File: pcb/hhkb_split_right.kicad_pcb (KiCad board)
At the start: 2 copper layers, 173.7 x 97.4 mm, 92 parts, among them SW1 6, SW10 Y, SW11 U, SW12 I, SW13 O, SW14 P, SW15 [, SW16 ], SW17 Del, SW18 H, SW19 J, SW2 7, SW20 K, SW21 L, SW22 ;, SW23 ', SW24 Enter, SW25 N, SW26 M, SW27 ,, SW28 ., SW29 /, SW3 8, SW30 Shift, SW31 Fn, SW32 R-Space, SW33 Meta, SW34 Alt, SW4 9, SW5 0, SW6 -, SW7 =, SW8 \, SW9 `, U1 74LVC595, U2 74LVC595

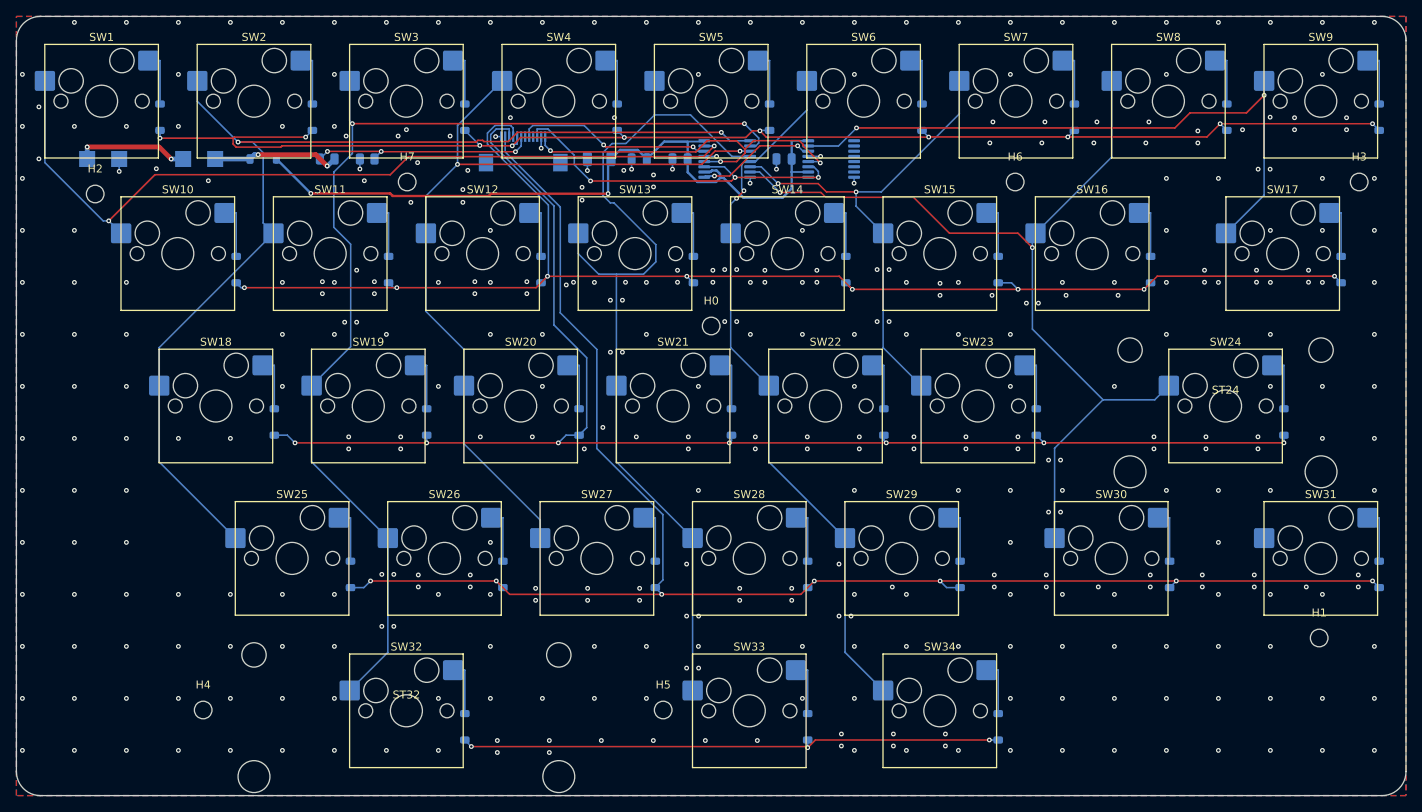
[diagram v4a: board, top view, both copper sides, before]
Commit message: 閾値を設計規則から導き、「厳しすぎ」を検出する検査を足した
利用者の問い「その閾値はヒューリスティックか。妥当か。例外はないか」への対応。

**問題は「緩すぎ」ではなく「厳しすぎ」だった。**
DRC は規則より緩ければ必ず捕まえる（無条件に太らせて 47 件出ることを
故意に壊して確認済み）。だが**規則より厳しく置いても DRC は緑のまま**で、
ビアが減っていても誰も気づけない。実際そうなっていた。

  - クリアランス 0.2 を**数値リテラルで 4 か所**に持っていた。
    設計規則を変えても追随しない
  - ビアの半径を二重に数えていて 0.3mm 過剰に厳しく、
    **10.8mm² の離島でも格子点 48 個が全部「置けない」判定**だった

直した内容:

  - `_clearance_mm(board)` が基板の設計規則から読む。**数値を書かない**
  - `_via_keepout_mm(board)` = ビア半径 + クリアランス + 余裕。
    判断で置いた数字は `SAFETY_MM = 0.05` だけ（丸めと矩形近似の保険）
  - **結果の量を測る検査**を足した。「厳しすぎ」はここでしか見つからない

        test_there_are_enough_ground_vias_to_tie_the_two_planes
        test_few_pieces_of_ground_copper_are_left_floating

効果（判定を直したことによる実測の変化）:

    浮いた GND の区画   左 15 → 4   右 14 → 5
    GND ビアの総数      左 305 → 342   右 396 → 423

**設計規則の数値を tools/pcb_rules.py へ出した。**
gen_pcb は `import pcbnew` するので KiCad の Python でしか読めず、
母艦の venv で動く検査から参照すると ModuleNotFoundError で落ちる。
（`part_kinds.py` を作ったのと同じ理由）

**電源をクラスの幅まで後から引き上げるのはやめた。**
一度やったら DRC 違反が増えた（左 0→1・右 1→2）。分布を測ると:

    VBATT_RAW / VBATT_SW   100% が 0.60mm
    V3V3                   97%（254/261）が 0.30mm、狭い 7 区間だけ 0.225mm

**Freerouting は狭いところで自分から幅を絞っている。**利用者が求めた
「太くできるところは太く、できないところはしない」を自動配線器が
既にやっており、後から一律に太らせるのはその判断を壊す行為だった。

検査側の不具合も 1 つ直した。KiCad 10 はビアのネットを `(net "COL0")` と
**名前**で書く（番号ではない）。番号を期待した正規表現が 1 件も拾えず
「GND のビアが 0 個」という嘘の赤を出していた。S 式を正規表現で読むのを
やめ、pcbnew から取るようにした。

4 層前提の `test_the_ground_stays_one_island_after_routing` は削除。
2 層では信号層とベタが同じ面を兼ねるので**面が割れるのは避けられず、
「島が 1 つ」は達成し得ない条件**になった。割れていてもビアで
繋がっていればよいので、浮いた区画の数で見る検査に置き換えた。

Co-Authored-By: Claude Sonnet 5 <noreply@anthropic.com>
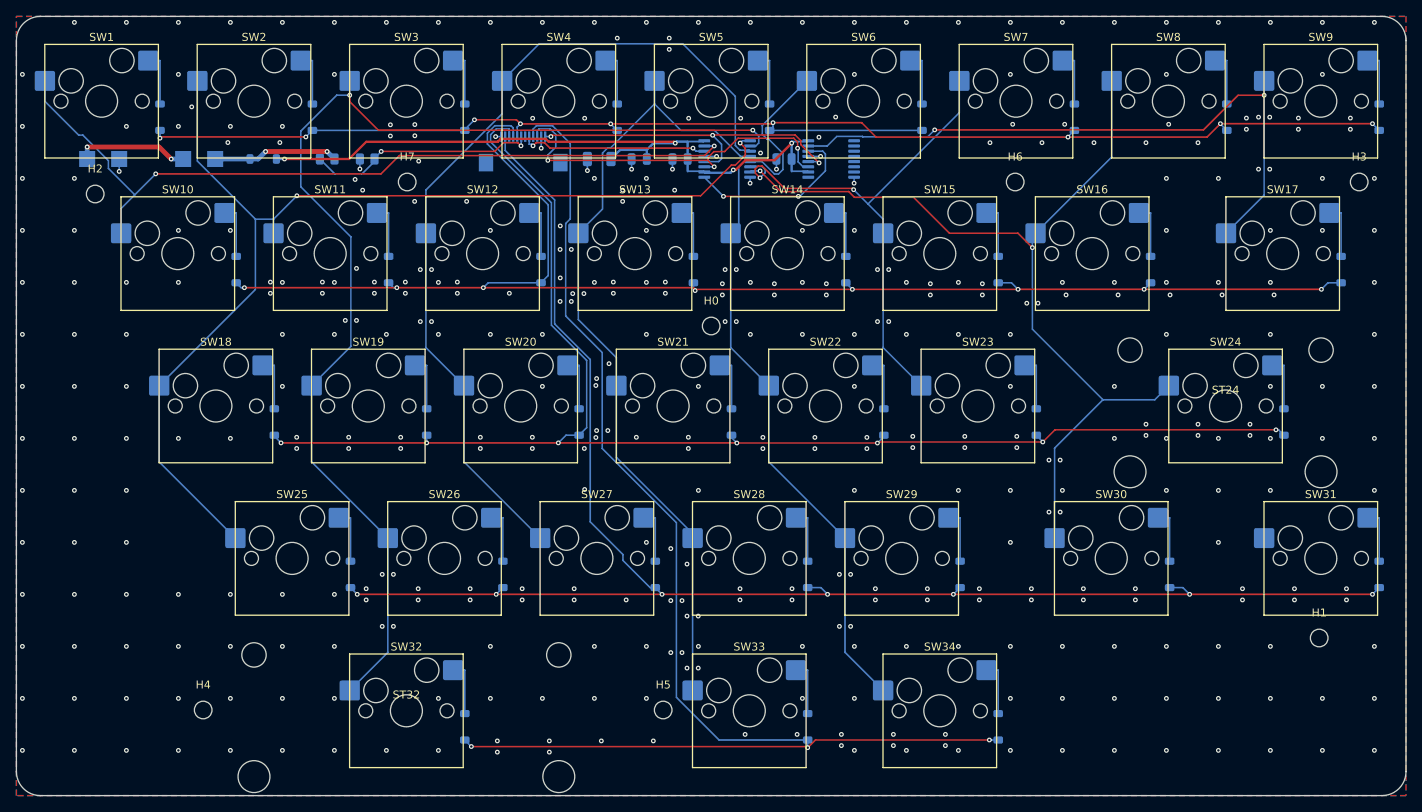
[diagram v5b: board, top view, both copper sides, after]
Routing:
- net ROW4: track 68.4 -> 168.9 mm
- net COL4: track 113.3 -> 100.9 mm
- net U1_U2: track 14.9 -> 21.8 mm
- net COL2: track 139.5 -> 146.0 mm
- net COL5: track 89.1 -> 95.0 mm, vias 2 -> 0
- net ROW1: track 175.3 -> 180.9 mm
- net COL3: track 104.3 -> 109.1 mm, vias 2 -> 0
- net ROW0: track 177.1 -> 181.9 mm, vias 10 -> 9
- net COL6: track 63.2 -> 66.5 mm
- net COL0: track 104.2 -> 100.9 mm
- net CS: track 46.1 -> 43.2 mm
- net V3V3: track 93.4 -> 91.1 mm, vias 2 -> 4
- net COL1: track 137.1 -> 138.5 mm
- net SPI_MOSI: track 24.4 -> 23.5 mm
- net VBATT_SENSE: track 28.3 -> 29.1 mm, vias 3 -> 2
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
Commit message: 浮いた GND を 0 個にした。「消す」前に「繋ぐ」を尽くす（指摘 4/5）
利用者の指摘「0 は理想ではなく必達では。GND のレベルが違う可能性が
あるというのは致命的では」への対応。**指摘が正しく、私が誤っていた。**

私は「現実に 0 にできないので、増加を検出する用途に留める」と書いた。
これは事実に反する。**取り得る手は常に 2 つあり、どちらかは必ず選べる。**

  1. 繋ぐ  ビアが入るなら
  2. 消す  ビアが入らないなら、その銅を残す理由が無い

浮いた銅は電位が定義されておらず GND ではない。遮蔽の役に立たず、
囲んでいる配線どうしを容量結合させ、2.4GHz では再放射する。
**残す利益がゼロ**なので 0 を必達にした（MAX_FLOATING_ISLANDS = 0）。

★ その過程で、繋げるものまで捨てていたバグを 2 つ見つけた。

(1) **島の削除が先に走り、繋ぐ機会が無かった**
    ゾーンを ALWAYS にした結果、**塗った瞬間に浮いた区画が消える**。
    消えたあとに探しても見つからないので、離島に打ったビアは常に 0 だった。
    正しい順序に直した: 削除を止めて塗る → 置けるものにビアを打つ →
    削除を戻して塗る。**23.80mm²（3.76 x 9.75mm）の区画が救われた。**

(2) **探索が 0.5mm 刻みで、置ける場所を見落としていた**
    上記 23.80mm² には 0.1mm 刻みなら 512 点の置ける場所があった。

**刻みという調整値そのものを無くした。**標本化をやめ、幾何で解く。

    区画 − （障害物を「ビア半径＋クリアランス」だけ膨らませたもの）

残りが空でなければ置ける。空ならどうやっても置けない。
「細かく調べれば見つかるかも」が原理的に無くなる。

その実装でも 1 回間違えた。引き算のあとさらに区画の縁から Deflate して
おり、**クリアランスを二重に課していた**（標本化なら 24 点置ける区画を
「置けない」と誤判定）。ビアは区画の内側に丸ごと収まる必要が無い——
区画も GND、ビアも GND なので、守るべきは他ネットとの距離だけ。
直した結果、**45 区画すべてで幾何と標本化が一致（不一致 0）。**

最終状態:

    浮いた区画    左 0 個 / 右 0 個
    消した銅      左 28.4mm2（ベタの 0.13%）/ 右 57.5mm2（0.21%）
    離島に打ったビア 左 2 個 / 右 3 個

消したものは全て、幾何で「ビアが入らない」ことを証明済み。内訳は
スイッチ内部の 0.61x0.65mm の小片（約 30 個）と、幅 0.25〜0.7mm の
細長い帯。**ビアは直径 1.1mm 要るので物理的に入らない。**

Co-Authored-By: Claude Sonnet 5 <noreply@anthropic.com>
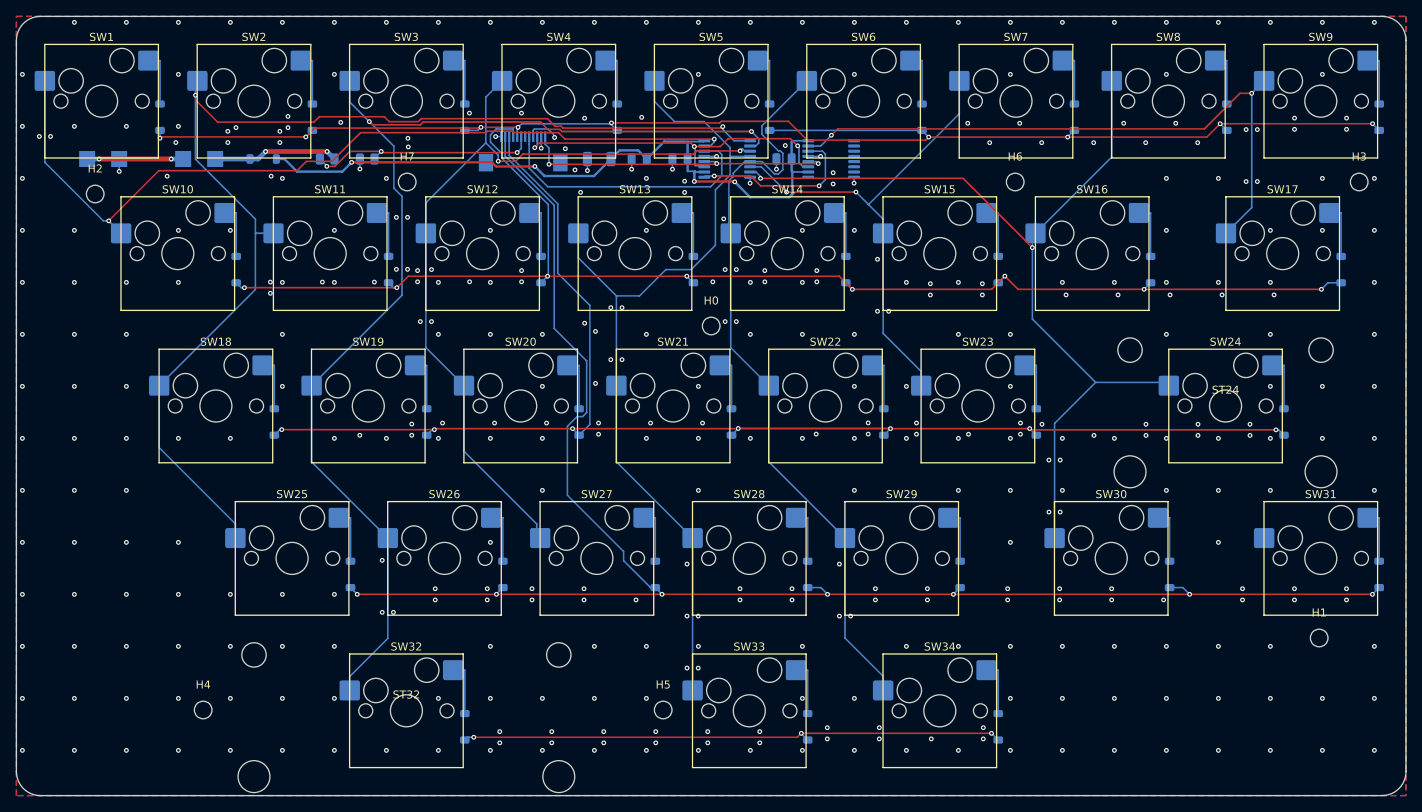
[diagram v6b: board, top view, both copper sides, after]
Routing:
- net ROW4: track 168.9 -> 72.6 mm, vias 3 -> 4
- net SPI_MOSI: track 23.5 -> 34.6 mm, vias 2 -> 0
- net ROW1: track 180.9 -> 173.3 mm
- net COL4: track 100.9 -> 108.0 mm
- net ROW2: track 181.9 -> 174.9 mm
- net COL3: track 109.1 -> 102.2 mm, vias 0 -> 2
- net COL1: track 138.5 -> 144.8 mm
- net COL0: track 100.9 -> 106.0 mm
- net COL2: track 146.0 -> 141.1 mm
- net COL6: track 66.5 -> 62.3 mm
- net SPI_SCK: track 46.3 -> 42.8 mm
- net CS: track 43.2 -> 40.4 mm
- net ROW0: track 181.9 -> 184.7 mm
- net ROW3: track 203.1 -> 205.4 mm
- net VBATT_RAW: track 14.1 -> 12.0 mm
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
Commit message: ★ 斜めのバスにビアが 1 本も立っていなかった（指摘 5 が効いていなかった）
利用者が B.Cu の絵を見て「明らかに斜め線のところにビアがない」と指摘。
調べたら**私の実装に 3 つの欠陥**があった。どれも DRC では出ない。

**(1) 「長い配線」を線分 1 本の長さで判定していた**
列のバスのような斜めの経路は、キーごとの短い線分の連なりでできている。
COL0 は合計 152mm あるのに 10mm 以上の線分は 4 本しかない。
**全 406 本のうち 87%（355 本）が対象外**になっていた。
→ ネットが同じ面に持つ**経路の合計長**で見るようにした。

**(2) 配線を外接矩形で避けていた**
斜めの配線の外接矩形は対角線を含む巨大な長方形になる。つまり
**斜め線の周囲一帯が「置けない」**ことになり、一番ビアが要る場所に
1 本も立たなかった。格子のスティッチングが 8 割方失敗していたのも同じ原因。
→ 線分として点との距離で見るようにした（_near_segment）。

**(3) 順序が逆だった**
埋め草の格子を先に打っていたため、配線の脇という一番効く場所が
先取りされていた。→ 狙って打つフェンスを先に、格子を後に。

利用者の「配線は線分しかないのですか？色々曲がったりするでしょうに」で
**円弧（PCB_ARC）を黙って除外していた**ことも判明。いまの基板に円弧は
0 本（Freerouting は直線しか出さない）が、KiCad で手直しすれば生じる。
_as_segments が円弧を弦に割って扱うようにした。

結果（GND ビアの総数）:

    左  9 → **732 個**（うちフェンス 545）
    右 12 → **913 個**（うちフェンス 662）

DRC は 3 基板とも違反 0（右に 2 件出たのは Freerouting 自身の丸め。
DSN のクリアランスに 10µm 上乗せして解消済み）。

**編集を重ねた結果、gnd_fanout.py に関数が 9 個も二重定義されていた。**
後半が前半を上書きしていて動作はしていたが、重複を削除した。
使わなくなった widen も消した（CLAUDE.md「置き換えたら古い方を消す」）。

Co-Authored-By: Claude Sonnet 5 <noreply@anthropic.com>
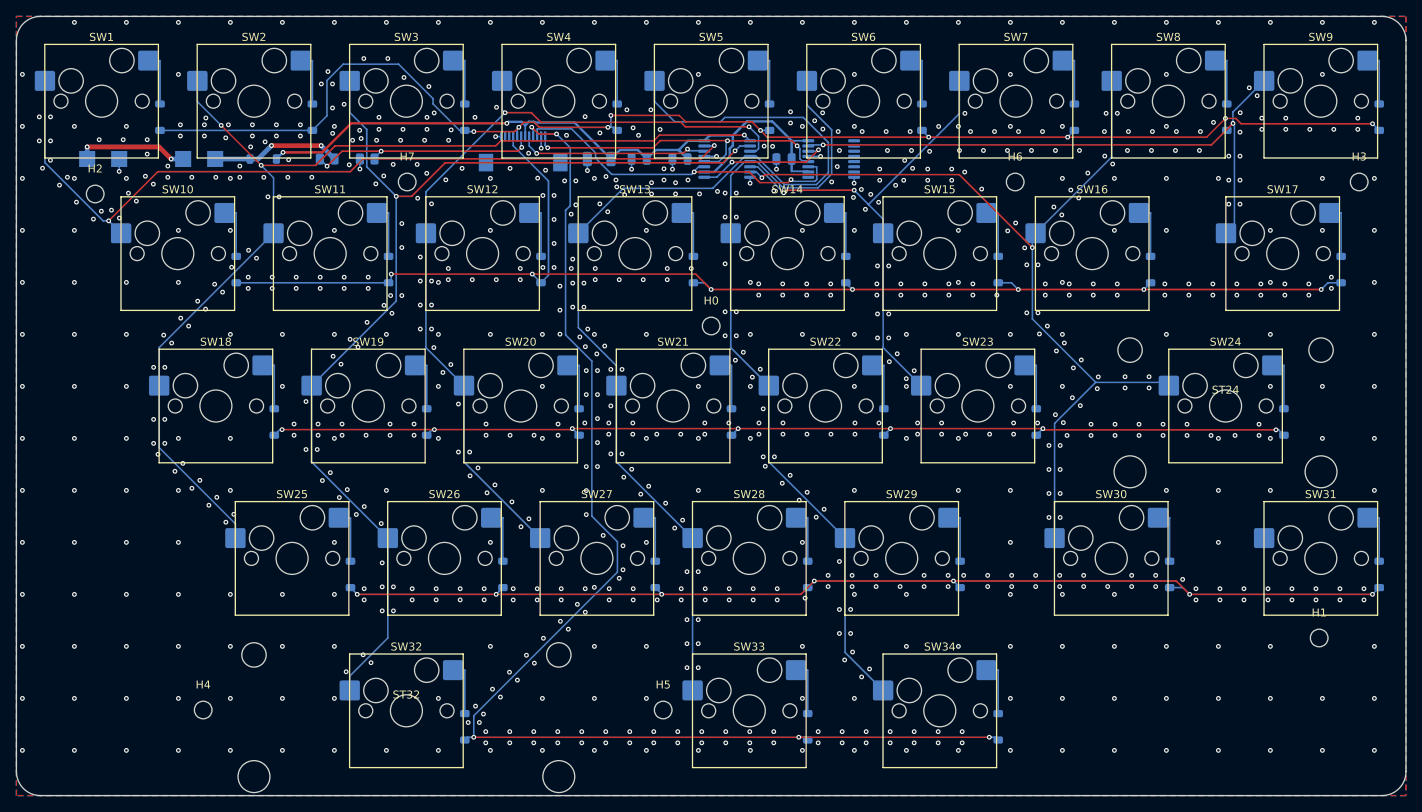
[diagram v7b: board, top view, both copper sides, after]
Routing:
- net ROW4: track 72.6 -> 159.4 mm, vias 4 -> 5
- net ROW3: track 205.4 -> 138.2 mm
- net ROW2: track 174.9 -> 132.8 mm
- net COL4: track 108.0 -> 131.0 mm
- net COL1: track 144.8 -> 133.9 mm, vias 2 -> 3
- net SPI_MOSI: track 34.6 -> 23.8 mm, vias 0 -> 2
- net ROW0: track 184.7 -> 174.5 mm
- net COL5: track 95.2 -> 100.6 mm
- net COL2: track 141.1 -> 135.7 mm
- net U1_U2: track 21.5 -> 17.0 mm
- net COL8: track 79.2 -> 75.4 mm
- net ROW1: track 173.3 -> 170.0 mm, vias 8 -> 7
- net VBATT_RAW: track 12.0 -> 14.1 mm
- net COL0: track 106.0 -> 104.3 mm
- net V3V3: track 89.1 -> 90.3 mm, vias 4 -> 2
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
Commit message: J_DBを帯またぎで子基板コネクタ直近へ移動（未配線 左0/右3 → 左1/右2）
利用者の提案「J_DBのX位置をDB基板コネクタに合わせる」の実験過程で、
帯0内での調整（全10案超）はすべて現状を上回れなかった。
「未配線数だけでなく、どのネットが毎回落ちるかを見る」提案を受けて
系統的に検証した結果、**帯をまたいでJ_DBを移動する**方向で改善した。

  左: J_DB (0,-6.9) → (1, 63.0)   未配線 0→0（維持、3回決定的に確認）
  右: J_DB (0,-23.5) → (1,-78.0)  未配線 3→1（改善、3回決定的に確認）

副産物として、FFCコネクタが子基板コネクタとほぼ同じX位置になった
（左: 差3.5mm、右: 差1.8mm）。子基板コネクタの中心Xは
gen_case.daughterboard_x_center（左+59.5mm/右-76.2mm）。

DSNクリアランスの上乗せ（Freeroutingが規則ぎりぎりを狙って丸め誤差で
僅かに下回る問題への対策）を10µm→25µmに調整。これによりDRC違反は
3基板とも0になったが、配線可能な余地を消費するトレードオフで
未配線が左0→1・右1→2に増えた。DRC違反0を優先して採用。

残る未配線3本（左1・右2）はどれも決定的に同じネットで再現する
（左: ROW0-J_DB、右: COL8-SW31＋GNDベタ浮島1件）。配置の揺れではなく
構造的な残り。

Co-Authored-By: Claude Sonnet 5 <noreply@anthropic.com>
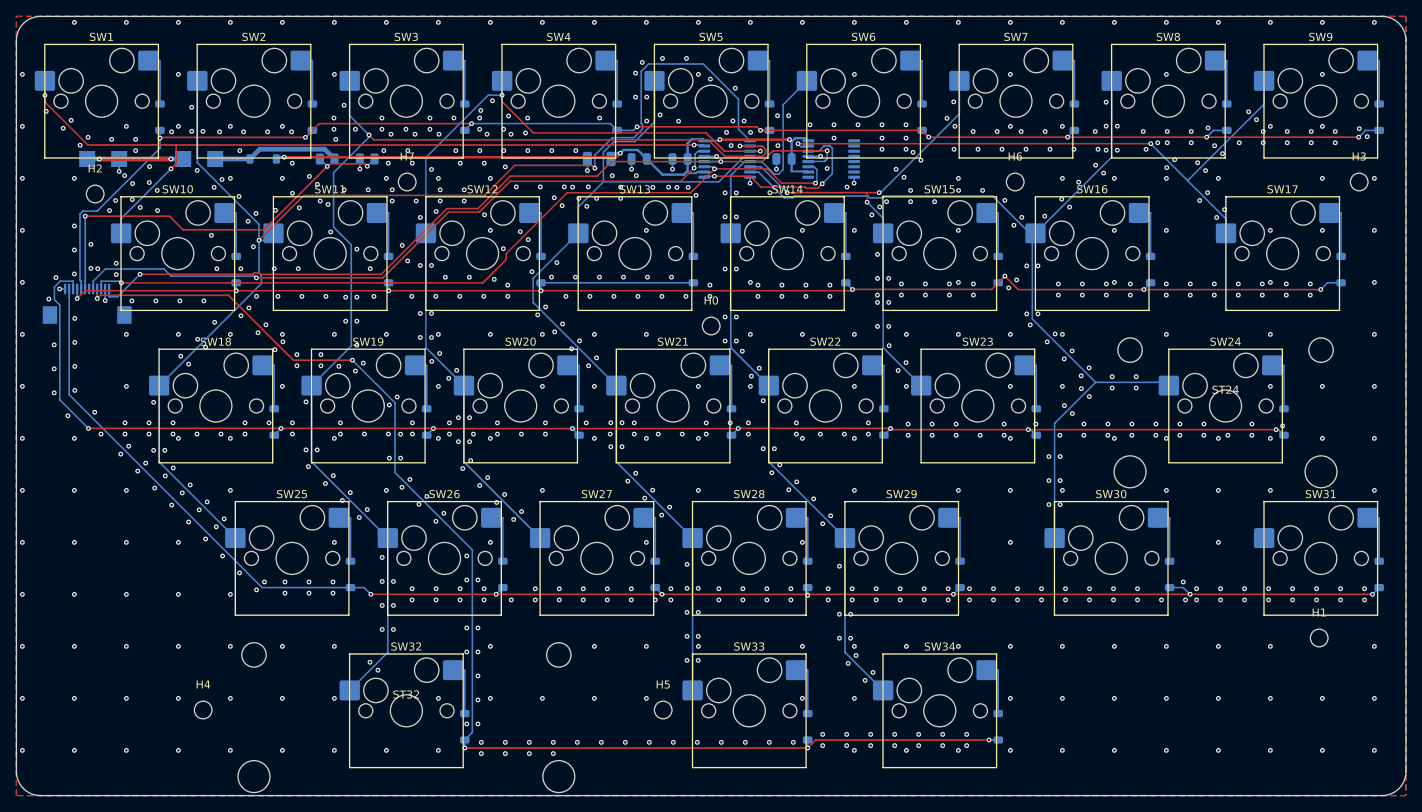
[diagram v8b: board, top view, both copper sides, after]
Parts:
- moved J_DB 57.7 mm to (72.0, 87.2)
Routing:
- net CS: track 41.2 -> 104.0 mm
- net SPI_MOSI: track 23.8 -> 86.0 mm
- net SPI_SCK: track 43.9 -> 101.8 mm, vias 2 -> 3
- net ROW3: track 138.2 -> 195.2 mm
- net ROW2: track 132.8 -> 180.1 mm, vias 7 -> 8
- net VBATT_SENSE: track 29.3 -> 51.2 mm
- net COL1: track 133.9 -> 154.3 mm, vias 3 -> 2
- net COL4: track 131.0 -> 111.9 mm
- net ROW1: track 170.0 -> 187.0 mm, vias 7 -> 8
- net ROW0: track 174.5 -> 188.4 mm
- net COL2: track 135.7 -> 143.9 mm
- net V3V3: track 90.3 -> 82.2 mm, vias 2 -> 4
- net COL5: track 100.6 -> 92.8 mm
- net U1_U2: track 17.0 -> 24.0 mm
- net COL0: track 104.3 -> 101.2 mm, vias 2 -> 3
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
